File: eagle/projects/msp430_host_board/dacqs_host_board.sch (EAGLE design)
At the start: 109 parts, among them J1 MOL-SL-4-RA, J10 MOL-SL-3-V, J12 MOL-SL-2-V, J13 JST-PH-2TH-RA, J14 USB_MICROB_RECPT, J16 MOL-SL-2-RA, J17 CLM-112-02-L-D, J18 MOLSL-7-RA, J2 MOL-SL-4-RA, J3 MOL-SL-4-RA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

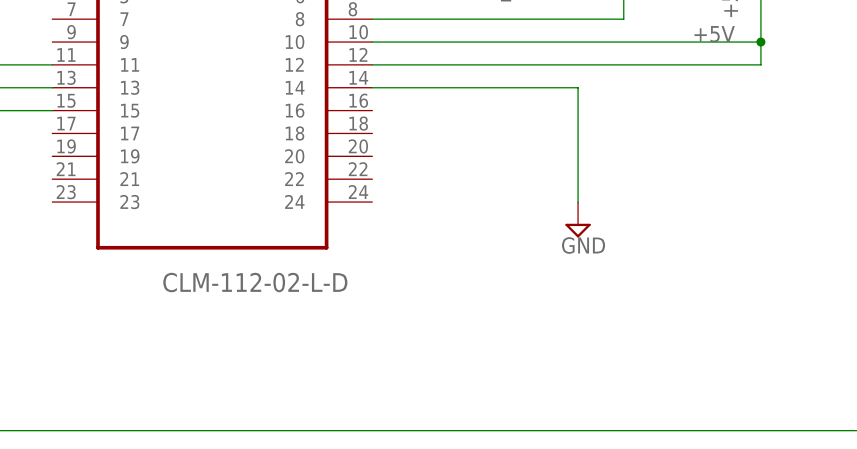
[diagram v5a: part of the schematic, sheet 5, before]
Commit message: Added IMU footprint to library and updated schematic part
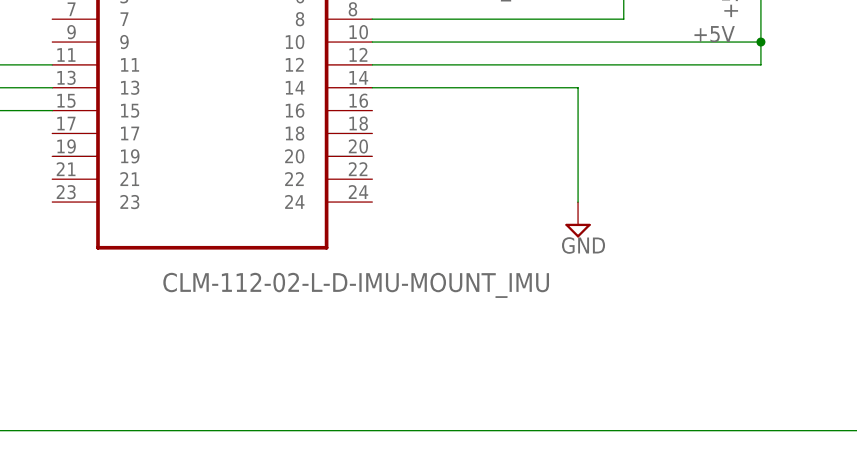
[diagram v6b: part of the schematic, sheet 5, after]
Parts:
- J17: value CLM-112-02-L-D -> CLM-112-02-L-D-IMU-MOUNT_IMU; device daqcs_host:CLM-112-02-L-D -> daqcs_host:CLM-112-02-L-D-IMU-MOUNT_IMU
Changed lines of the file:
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@@
 <part name="R29" library="daqcs_host" deviceset="RES" device="_0603" technology="_27R0" value="27k"/>
 <part name="SUPPLY32" library="supply2" deviceset="GND" device=""/>
-<part name="J17" library="daqcs_host" deviceset="CLM-112-02-L-D" device=""/>
 <part name="J11" library="daqcs_host" deviceset="M02" device="PTH"/>
 <part name="+3V14" library="supply1" deviceset="+3V3" device=""/>
@@
 <part name="C27" library="daqcs_host" deviceset="CAP" device="_0603" technology="_100NF0" value="100nF"/>
 <part name="J18" library="daqcs_host" deviceset="MOLSL_7PIN" device="_RA" value="MOLSL-7-RA"/>
+<part name="J17" library="daqcs_host" deviceset="CLM-112-02-L-D-IMU-MOUNT" device="_IMU"/>
 </parts>
 <sheets>
@@
 <instance part="SUPPLY18" gate="GND" x="269.24" y="43.18"/>
 <instance part="SUPPLY19" gate="GND" x="271.78" y="99.06" rot="R180"/>
+<instance part="J11" gate="G$1" x="172.72" y="93.98" rot="R180"/>
 <instance part="J17" gate="A" x="93.98" y="78.74"/>
-<instance part="J11" gate="G$1" x="172.72" y="93.98" rot="R180"/>
 </instances>
 <busses>
@@
 <wire x1="139.7" y1="81.28" x2="139.7" y2="93.98" width="0.1524" layer="91"/>
 <wire x1="139.7" y1="93.98" x2="165.1" y2="93.98" width="0.1524" layer="91"/>
+<pinref part="J11" gate="G$1" pin="1"/>
 <pinref part="J17" gate="A" pin="8"/>
-<pinref part="J11" gate="G$1" pin="1"/>
-</segment>
-</net>
+</segment>
+</net>

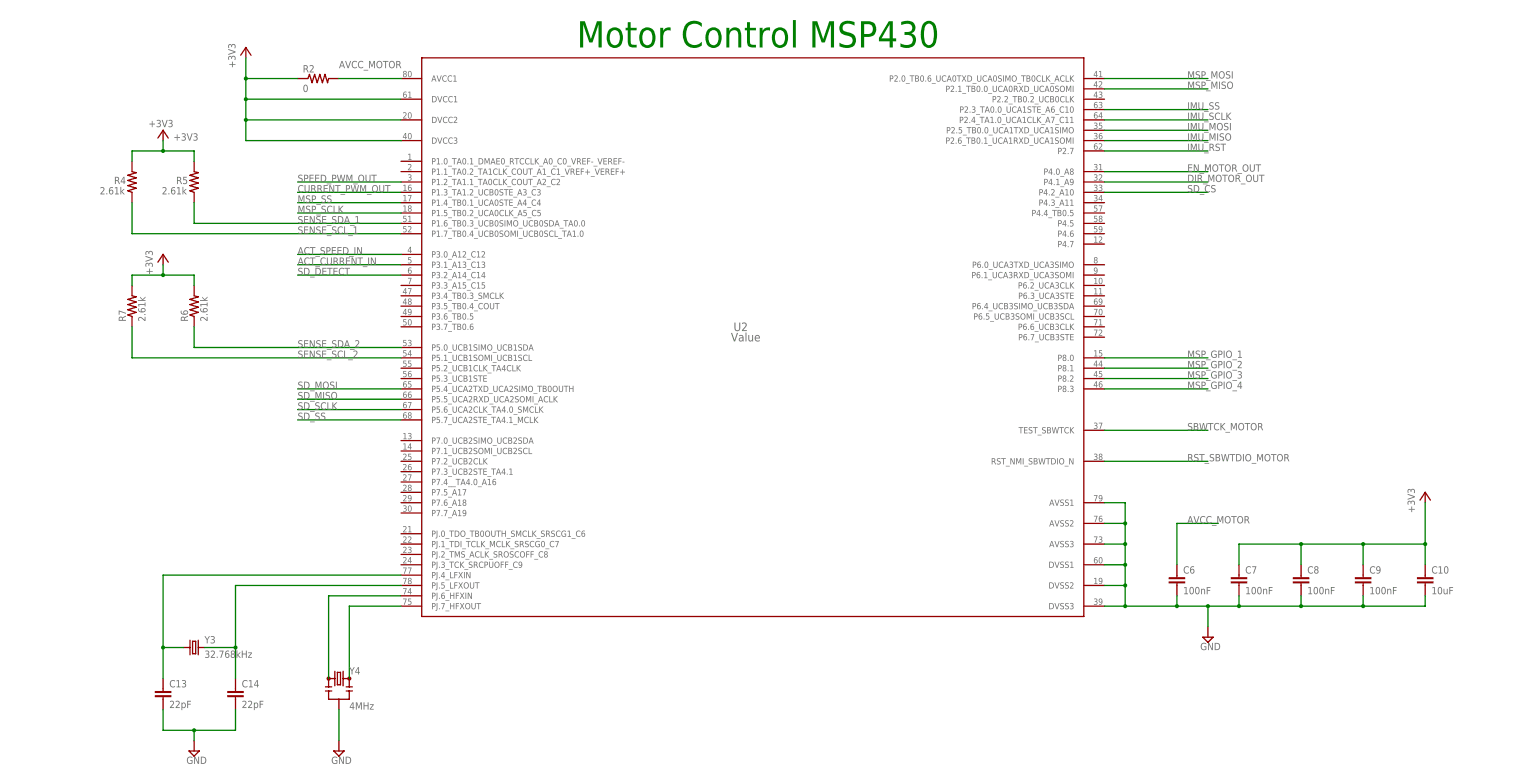
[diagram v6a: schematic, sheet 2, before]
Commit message: Added status LEDs to MSP430s names to all nets
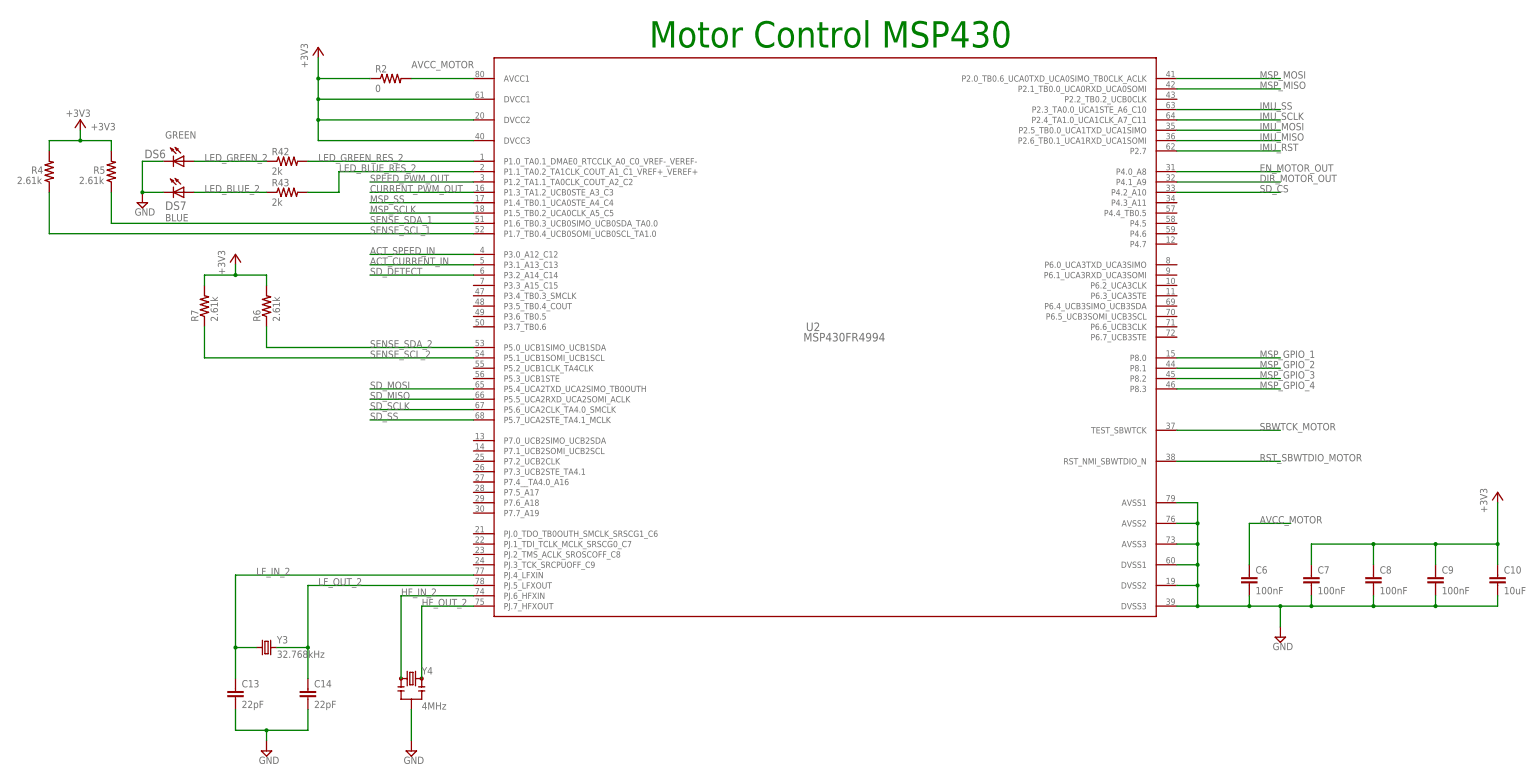
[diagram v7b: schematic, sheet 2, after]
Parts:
- added DS4, DS6: GREEN, daqcs_host:LED_G3V2WURTH_0603
- added DS5, DS7: BLUE, daqcs_host:LED_B3V2WURTH_0603
- added R26, R27, R42, R43: 2k, daqcs_host:RES_2R0_0603
- U1, U2: value Value -> MSP430FR4994
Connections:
- net N$1 renamed HF_OUT_1
- net N$2 renamed HF_IN_1
- net N$22 renamed TEMP_I2C_A0
- net N$23 renamed TEMP_I2C_A1
- net N$24 renamed TEMP_I2C_A2
- net N$25 renamed OVER_TEMP_SHUTDOWN
- net N$3 renamed LF_OUT_1
- net N$32 renamed IMU_RST_2
- net N$36 renamed VBAT_IN
- net N$38 renamed SHIELD_GND
- net N$39 renamed VBAT_POS_RETURN
- net N$4 renamed LF_IN_1
- net N$40 renamed VBAT_POS
- net N$41 renamed VBAT_READY
- net N$42 renamed BATT_CHARGE_STAT
- net N$43 renamed VBAT_CHARGING
- net N$44 renamed PROG_REGULATION
- net N$45 renamed CURRENT_I2C_A0
- net N$46 renamed CURRENT_I2C_A1
- net N$6 renamed LF_IN_2
- net N$7 renamed LF_OUT_2
- net N$8 renamed HF_IN_2
- net N$9 renamed HF_OUT_2
- removed net N$26: R12.2
- new net IMU_RST_1: J11.2
- new net LED_BLUE_1: DS5.A, R27.1
- new net LED_BLUE_2: DS7.A, R43.1
- new net LED_BLUE_RES_1: R27.2, U1.P1.1_TA0.2_TA1CLK_COUT_A1_C1_VREF+_VEREF+
- new net LED_BLUE_RES_2: R43.2, U2.P1.1_TA0.2_TA1CLK_COUT_A1_C1_VREF+_VEREF+
- new net LED_GREEN_1: DS4.A, R26.1
- new net LED_GREEN_2: DS6.A, R42.1
- new net LED_GREEN_RES_1: R26.2, U1.P1.0_TA0.1_DMAE0_RTCCLK_A0_C0_VREF-_VEREF-
- new net LED_GREEN_RES_2: R42.2, U2.P1.0_TA0.1_DMAE0_RTCCLK_A0_C0_VREF-_VEREF-
- net GND: now also DS4.C, DS5.C, DS6.C, DS7.C
- net IMU_RST: no longer J11.2
- net VBAT_MOD_CELL_1: now also U1.P3.1_A13_C13
- net VBAT_MOD_CELL_2: now also U1.P3.2_A14_C14
- net VBAT_MOD_CELL_3: now also U1.P3.3_A15_C15
- net VBAT_MOD_CELL_4: now also U1.P7.5_A17
- net VBAT_MOD_CELL_5: now also U1.P7.6_A18
- net VBAT_MOD_CELL_6: now also U1.P7.7_A19
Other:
- moved on the sheet: C10, C13, C14, C6, C7, C8, C9, DS1, DS2, J13, R10, R11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

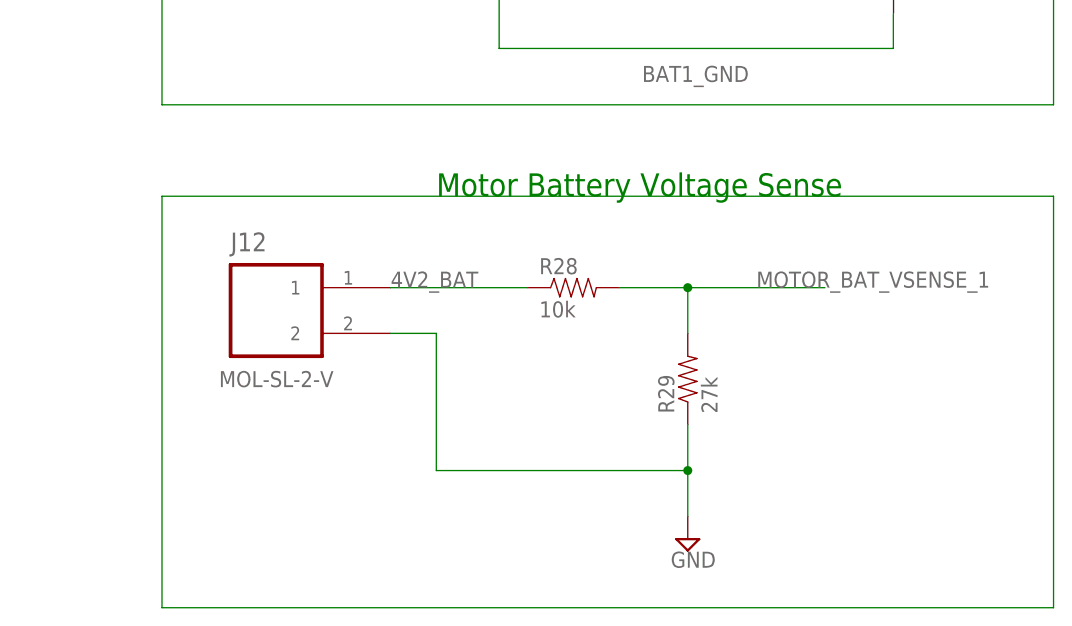
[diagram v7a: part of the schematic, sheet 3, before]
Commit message: Deleted old reaction wheel battery volatge sense
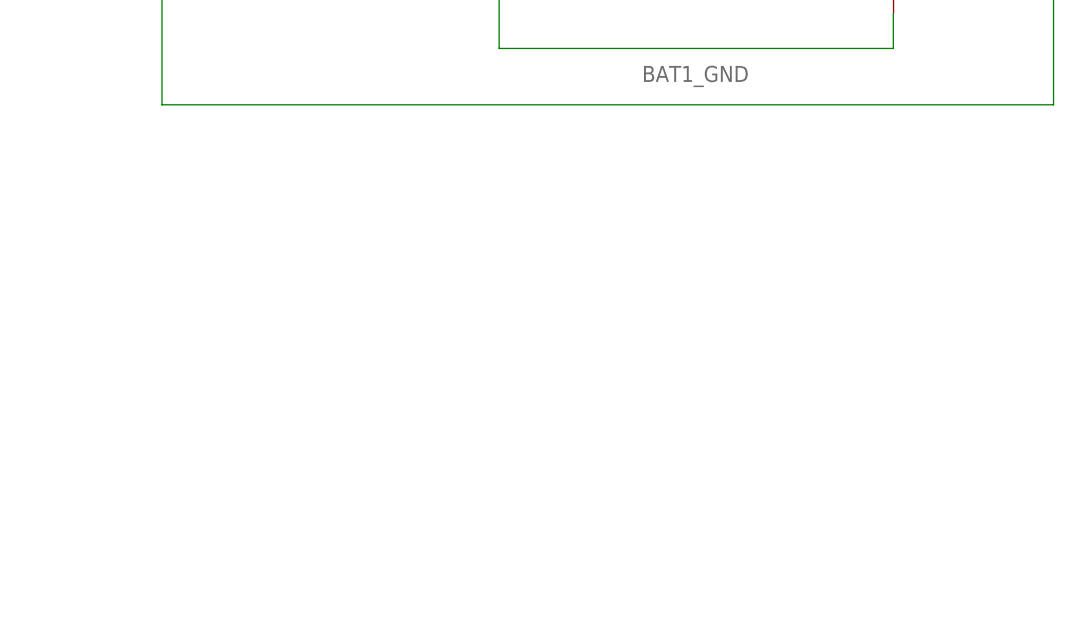
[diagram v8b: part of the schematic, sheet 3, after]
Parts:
- removed J12: MOL-SL-2-V, daqcs_host:MOLSL_2PIN_SL2V_V
- removed R28: 10k, daqcs_host:RES_10R0_0603
- removed R29: 27k, daqcs_host:RES_27R0_0603
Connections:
- removed net 4V2_BAT: J12.1, R28.1
- removed net MOTOR_BAT_VSENSE_1: R28.2, R29.2, U1.P3.0_A12_C12
- net GND: no longer J12.2, R29.1
- net VBAT_MOD_CELL_1: now also U1.P3.0_A12_C12; no longer U1.P3.1_A13_C13
- net VBAT_MOD_CELL_2: now also U1.P3.1_A13_C13; no longer U1.P3.2_A14_C14
- net VBAT_MOD_CELL_3: now also U1.P3.2_A14_C14; no longer U1.P3.3_A15_C15
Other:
- note removed: "Motor Battery Voltage Sense"
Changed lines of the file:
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@@
 <setting verticaltext="up"/>
 </settings>
-<grid distance="0.1" unitdist="inch" unit="inch" style="lines" multiple="1" display="yes" altdistance="0.01" altunitdist="inch" altunit="inch"/>
+<grid distance="0.1" unitdist="inch" unit="inch" style="lines" multiple="1" display="no" altdistance="0.01" altunitdist="inch" altunit="inch"/>
 <layers>
 <layer number="1" name="Top" color="4" fill="1" visible="no" active="no"/>
@@
 <part name="U9" library="daqcs_host" deviceset="STD12NF06LT4" device=""/>
 <part name="BAT1" library="daqcs_host" deviceset="BC9VPC" device="" value="9V"/>
-<part name="R28" library="daqcs_host" deviceset="RES" device="_0603" technology="_10R0" value="10k"/>
-<part name="R29" library="daqcs_host" deviceset="RES" device="_0603" technology="_27R0" value="27k"/>
-<part name="SUPPLY32" library="supply2" deviceset="GND" device=""/>
 <part name="J11" library="daqcs_host" deviceset="M02" device="PTH"/>
 <part name="+3V14" library="supply1" deviceset="+3V3" device=""/>
@@
 <part name="J5" library="daqcs_host" deviceset="MOLSL_5PIN" device="_RA" technology="_SL4RA" value="MOL-SL-5-RA"/>
 <part name="J6" library="daqcs_host" deviceset="MOLSL_3PIN" device="_V" technology="_SL3V" value="MOL-SL-3-V"/>
-<part name="J12" library="daqcs_host" deviceset="MOLSL_2PIN" device="_V" technology="_SL2V" value="MOL-SL-2-V"/>
 <part name="J16" library="daqcs_host" deviceset="MOLSL_2PIN" device="_RA" technology="_SL2RA" value="MOL-SL-2-RA"/>
 <part name="J7" library="daqcs_host" deviceset="MOLSL_5PIN" device="_V" technology="_SL4V" value="MOL-SL-5-V"/>
@@
 </segment>
 </net>
-<net name="MOTOR_BAT_VSENSE_1" class="0">
+<net name="VBAT_MOD_CELL_1" class="0">
 <segment>
 <pinref part="U1" gate="A" pin="P3.0_A12_C12"/>
 <wire x1="55.88" y1="149.86" x2="30.48" y2="149.86" width="0.1524" layer="91"/>
-<label x="27.94" y="149.86" size="1.778" layer="95"/>
-</segment>
-</net>
-<net name="VBAT_MOD_CELL_1" class="0">
+<label x="30.48" y="149.86" size="1.778" layer="95"/>
+</segment>
+</net>
+<net name="VBAT_MOD_CELL_2" class="0">
 <segment>
 <pinref part="U1" gate="A" pin="P3.1_A13_C13"/>
@@
 </segment>
 </net>
-<net name="VBAT_MOD_CELL_2" class="0">
+<net name="VBAT_MOD_CELL_3" class="0">
 <segment>
 <pinref part="U1" gate="A" pin="P3.2_A14_C14"/>
 <wire x1="55.88" y1="144.78" x2="30.48" y2="144.78" width="0.1524" layer="91"/>
 <label x="30.48" y="144.78" size="1.778" layer="95"/>
-</segment>
-</net>
-<net name="VBAT_MOD_CELL_3" class="0">
-<segment>
-<pinref part="U1" gate="A" pin="P3.3_A15_C15"/>
-<wire x1="55.88" y1="142.24" x2="30.48" y2="142.24" width="0.1524" layer="91"/>
-<label x="30.48" y="142.24" size="1.778" layer="95"/>
 </segment>
 </net>
@@
 <text x="231.14" y="152.4" size="2.54" layer="91">Cutdown Switch and Connector</text>
 <text x="111.76" y="233.68" size="6.4516" layer="91">Host MSP430 Connectors</text>
-<text x="236.22" y="81.28" size="2.54" layer="91">Motor Battery Voltage Sense</text>
 </plain>
 <instances>
@@
 <instance part="U9" gate="A" x="236.22" y="114.3"/>
 <instance part="BAT1" gate="G$1" x="287.02" y="111.76"/>
-<instance part="R28" gate="G$1" x="251.46" y="71.12"/>
-<instance part="R29" gate="G$1" x="264.16" y="60.96" rot="R90"/>
-<instance part="SUPPLY32" gate="GND" x="264.16" y="43.18"/>
 <instance part="J1" gate="G$1" x="20.32" y="195.58"/>
 <instance part="J2" gate="G$1" x="99.06" y="195.58"/>
@@
 <instance part="J5" gate="G$1" x="20.32" y="78.74"/>
 <instance part="J6" gate="G$1" x="99.06" y="83.82"/>
-<instance part="J12" gate="G$1" x="218.44" y="68.58"/>
 <instance part="J16" gate="G$1" x="266.7" y="142.24" rot="R270"/>
 </instances>
@@
 <label x="121.92" y="78.74" size="1.778" layer="95"/>
 <pinref part="J6" gate="G$1" pin="3"/>
-</segment>
-<segment>
-<wire x1="231.14" y1="66.04" x2="236.22" y2="66.04" width="0.1524" layer="91"/>
-<wire x1="236.22" y1="66.04" x2="236.22" y2="50.8" width="0.1524" layer="91"/>
-<pinref part="R29" gate="G$1" pin="1"/>
-<wire x1="236.22" y1="50.8" x2="264.16" y2="50.8" width="0.1524" layer="91"/>
-<wire x1="264.16" y1="50.8" x2="264.16" y2="55.88" width="0.1524" layer="91"/>
-<pinref part="SUPPLY32" gate="GND" pin="GND"/>
-<wire x1="264.16" y1="45.72" x2="264.16" y2="50.8" width="0.1524" layer="91"/>
-<junction x="264.16" y="50.8"/>
-<pinref part="J12" gate="G$1" pin="2"/>
 </segment>
 </net>
@@
 </segment>
 </net>
-<net name="4V2_BAT" class="0">
-<segment>
-<pinref part="R28" gate="G$1" pin="1"/>
-<wire x1="231.14" y1="71.12" x2="246.38" y2="71.12" width="0.1524" layer="91"/>
-<label x="231.14" y="71.12" size="1.778" layer="95"/>
-<pinref part="J12" gate="G$1" pin="1"/>
-</segment>
-</net>
-<net name="MOTOR_BAT_VSENSE_1" class="0">
-<segment>
-<pinref part="R28" gate="G$1" pin="2"/>
-<pinref part="R29" gate="G$1" pin="2"/>
-<wire x1="256.54" y1="71.12" x2="264.16" y2="71.12" width="0.1524" layer="91"/>
-<wire x1="264.16" y1="71.12" x2="264.16" y2="66.04" width="0.1524" layer="91"/>
-<wire x1="264.16" y1="71.12" x2="279.4" y2="71.12" width="0.1524" layer="91"/>
-<junction x="264.16" y="71.12"/>
-<label x="271.78" y="71.12" size="1.778" layer="95"/>
-</segment>
-</net>
-<net name="N$54" class="0">
-<segment>
-<wire x1="205.74" y1="81.28" x2="304.8" y2="81.28" width="0.1524" layer="91"/>
-<wire x1="304.8" y1="81.28" x2="304.8" y2="35.56" width="0.1524" layer="91"/>
-<wire x1="304.8" y1="35.56" x2="205.74" y2="35.56" width="0.1524" layer="91"/>
-<wire x1="205.74" y1="35.56" x2="205.74" y2="81.28" width="0.1524" layer="91"/>
-</segment>
-</net>
